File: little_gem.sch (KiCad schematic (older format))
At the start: 11 parts, among them J1 AudioPlug2, U1 LM386

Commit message: Finished sch and pcb
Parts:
- C1, C2, C3: footprint (none) -> Capacitor_THT:C_Rect_L7.2mm_W2.5mm_P5.00mm_FKS2_FKP2_MKS2_MKP2
- C4: value 47 -> 47n; footprint (none) -> Capacitor_THT:C_Rect_L7.2mm_W2.5mm_P5.00mm_FKS2_FKP2_MKS2_MKP2
- C5: value 220n -> 220u; footprint (none) -> Capacitor_THT:CP_Radial_D6.3mm_P2.50mm
- J1: footprint (none) -> Connector_PinHeader_1.00mm:PinHeader_1x02_P1.00mm_Vertical_audio_jack
- LS1: renamed from LS?; footprint (none) -> Connector_PinHeader_1.00mm:PinHeader_1x02_P1.00mm_Vertical
- R1: footprint (none) -> Resistor_THT:R_Axial_DIN0207_L6.3mm_D2.5mm_P10.16mm_Horizontal
- R_GAIN1: renamed from RV1; footprint (none) -> Connector_PinHeader_1.00mm:PinHeader_1x03_P1.00mm_Vertical
- R_VOLUME1: renamed from RV2; footprint (none) -> Connector_PinHeader_1.00mm:PinHeader_1x03_P1.00mm_Vertical
- U1: footprint (none) -> Package_DIP:DIP-8_W7.62mm_Socket_LongPads
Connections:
- net labels added: GND
- net labels removed: GNDA

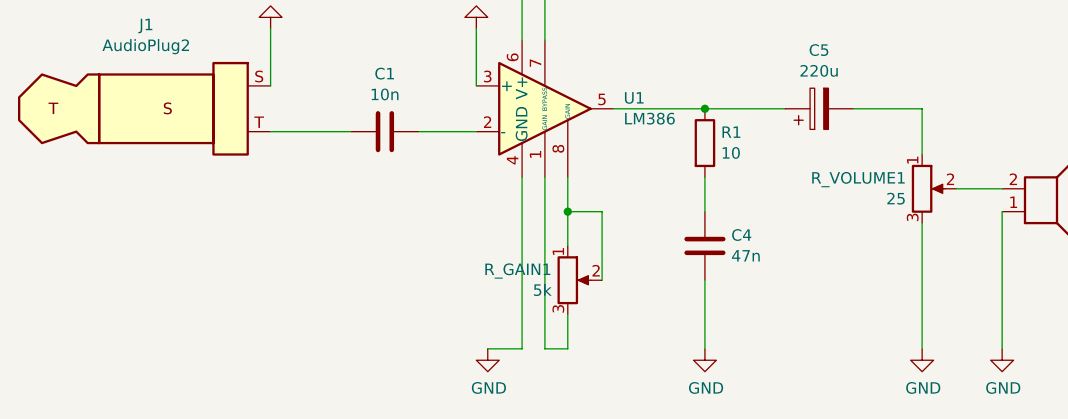
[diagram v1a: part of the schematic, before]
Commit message: replaced footprints for pots and connectors
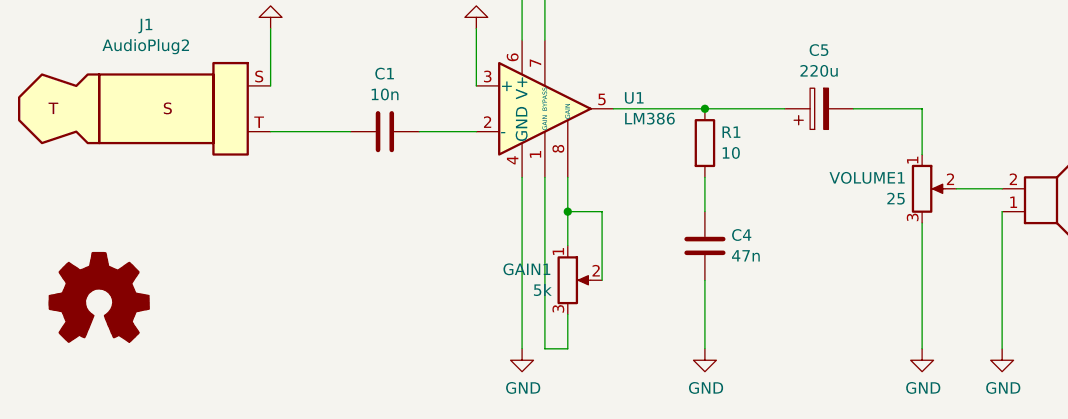
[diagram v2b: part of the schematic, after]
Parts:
- GAIN1: renamed from R_GAIN1; footprint Connector_PinHeader_1.00mm:PinHeader_1x03_P1.00mm_Vertical -> Connector_PinHeader_2.00mm:PinHeader_1x03_P2.00mm_Vertical
- J1: footprint Connector_PinHeader_1.00mm:PinHeader_1x02_P1.00mm_Vertical_audio_jack -> Connector_PinHeader_2.00mm:PinHeader_1x02_P2.00mm_Vertical_LittleGem
- LS1: footprint Connector_PinHeader_1.00mm:PinHeader_1x02_P1.00mm_Vertical -> Connector_PinHeader_2.00mm:PinHeader_1x02_P2.00mm_Vertical
- VOLUME1: renamed from R_VOLUME1; footprint Connector_PinHeader_1.00mm:PinHeader_1x03_P1.00mm_Vertical -> Connector_PinHeader_2.00mm:PinHeader_1x03_P2.00mm_Vertical
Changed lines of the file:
@@
 $EndComp
 $Comp
-L Device:R_POT R_VOLUME1
+L Device:R_POT VOLUME1
 U 1 1 5EF07295
 P 6650 4250
-F 0 "R_VOLUME1" H 6580 4296 50  0000 R CNN
+F 0 "VOLUME1" H 6580 4296 50  0000 R CNN
 F 1 "25" H 6580 4205 50  0000 R CNN
-F 2 "Connector_PinHeader_1.00mm:PinHeader_1x03_P1.00mm_Vertical" H 6650 4250 50  0001 C CNN
+F 2 "Connector_PinHeader_2.00mm:PinHeader_1x03_P2.00mm_Vertical" H 6650 4250 50  0001 C CNN
 F 3 "~" H 6650 4250 50  0001 C CNN
 	1    6650 4250
@@
 	4900 4200 4900 4950
 Wire Wire Line
-	4900 4950 4750 4950
-Wire Wire Line
 	5700 4950 5700 4650
 Wire Wire Line
@@
 	5000 2450 5000 2750
 $Comp
-L power:+9V #PWR0109
+L power:+9V #PWR03
 U 1 1 5EF30250
 P 3950 2750
-F 0 "#PWR0109" H 3950 2600 50  0001 C CNN
+F 0 "#PWR03" H 3950 2600 50  0001 C CNN
 F 1 "+9V" V 3965 2878 50  0000 L CNN
 F 2 "" H 3950 2750 50  0001 C CNN
@@
 	4450 2750 4900 2750
 $Comp
-L power:GND #PWR0102
+L power:GND #PWR07
 U 1 1 5EF434C2
-P 4750 4950
-F 0 "#PWR0102" H 4750 4700 50  0001 C CNN
-F 1 "GND" H 4755 4777 50  0000 C CNN
-F 2 "" H 4750 4950 50  0001 C CNN
-F 3 "" H 4750 4950 50  0001 C CNN
-	1    4750 4950
-	1    0    0    -1
-$EndComp
-$Comp
-L power:GND #PWR0103
+P 4900 4950
+F 0 "#PWR07" H 4900 4700 50  0001 C CNN
+F 1 "GND" H 4905 4777 50  0000 C CNN
+F 2 "" H 4900 4950 50  0001 C CNN
+F 3 "" H 4900 4950 50  0001 C CNN
+	1    4900 4950
+	1    0    0    -1
+$EndComp
+$Comp
+L power:GND #PWR09
 U 1 1 5EF44012
 P 5700 4950
-F 0 "#PWR0103" H 5700 4700 50  0001 C CNN
+F 0 "#PWR09" H 5700 4700 50  0001 C CNN
 F 1 "GND" H 5705 4777 50  0000 C CNN
 F 2 "" H 5700 4950 50  0001 C CNN
@@
 $EndComp
 $Comp
-L power:GND #PWR0104
+L power:GND #PWR010
 U 1 1 5EF44713
 P 6650 4950
-F 0 "#PWR0104" H 6650 4700 50  0001 C CNN
+F 0 "#PWR010" H 6650 4700 50  0001 C CNN
 F 1 "GND" H 6655 4777 50  0000 C CNN
 F 2 "" H 6650 4950 50  0001 C CNN
@@
 $EndComp
 $Comp
-L power:GND #PWR0105
+L power:GND #PWR011
 U 1 1 5EF44C47
 P 7000 4950
-F 0 "#PWR0105" H 7000 4700 50  0001 C CNN
+F 0 "#PWR011" H 7000 4700 50  0001 C CNN
 F 1 "GND" H 7005 4777 50  0000 C CNN
 F 2 "" H 7000 4950 50  0001 C CNN
@@
 $EndComp
 $Comp
-L power:GND #PWR0108
+L power:GND #PWR08
 U 1 1 5EF45800
 P 5000 2450
-F 0 "#PWR0108" H 5000 2200 50  0001 C CNN
+F 0 "#PWR08" H 5000 2200 50  0001 C CNN
 F 1 "GND" H 5005 2277 50  0000 C CNN
 F 2 "" H 5000 2450 50  0001 C CNN
@@
 $EndComp
 $Comp
-L power:GND #PWR0107
+L power:GND #PWR06
 U 1 1 5EF4907C
 P 4700 3550
-F 0 "#PWR0107" H 4700 3300 50  0001 C CNN
+F 0 "#PWR06" H 4700 3300 50  0001 C CNN
 F 1 "GND" H 4705 3377 50  0000 C CNN
 F 2 "" H 4700 3550 50  0001 C CNN
@@
 $EndComp
 $Comp
-L power:GND #PWR0101
+L power:GND #PWR05
 U 1 1 5EF4B5A8
 P 4450 3200
-F 0 "#PWR0101" H 4450 2950 50  0001 C CNN
+F 0 "#PWR05" H 4450 2950 50  0001 C CNN
 F 1 "GND" H 4455 3027 50  0000 C CNN
 F 2 "" H 4450 3200 50  0001 C CNN
@@
 $EndComp
 $Comp
-L power:GND #PWR0106
+L power:GND #PWR01
 U 1 1 5EF4EC5F
 P 3800 3550
-F 0 "#PWR0106" H 3800 3300 50  0001 C CNN
+F 0 "#PWR01" H 3800 3300 50  0001 C CNN
 F 1 "GND" H 3805 3377 50  0000 C CNN
 F 2 "" H 3800 3550 50  0001 C CNN
@@
 $EndComp
 $Comp
-L power:PWR_FLAG #FLG0101
+L power:PWR_FLAG #FLG01
 U 1 1 5EF5745A
 P 3950 1400
-F 0 "#FLG0101" H 3950 1475 50  0001 C CNN
+F 0 "#FLG01" H 3950 1475 50  0001 C CNN
 F 1 "PWR_FLAG" H 3950 1573 50  0000 C CNN
 F 2 "" H 3950 1400 50  0001 C CNN
@@
 $EndComp
 $Comp
-L power:PWR_FLAG #FLG0102
+L power:PWR_FLAG #FLG02
 U 1 1 5EF57882
 P 4300 1400
-F 0 "#FLG0102" H 4300 1475 50  0001 C CNN
+F 0 "#FLG02" H 4300 1475 50  0001 C CNN
 F 1 "PWR_FLAG" H 4300 1573 50  0000 C CNN
 F 2 "" H 4300 1400 50  0001 C CNN
@@
 $EndComp
 $Comp
-L power:+9V #PWR0110
+L power:+9V #PWR02
 U 1 1 5EF57D46
 P 3950 1400
-F 0 "#PWR0110" H 3950 1250 50  0001 C CNN
+F 0 "#PWR02" H 3950 1250 50  0001 C CNN
 F 1 "+9V" V 3965 1528 50  0000 L CNN
 F 2 "" H 3950 1400 50  0001 C CNN
@@
 $EndComp
 $Comp
-L power:GND #PWR0111
+L power:GND #PWR04
 U 1 1 5EF585B3
 P 4300 1400
-F 0 "#PWR0111" H 4300 1150 50  0001 C CNN
+F 0 "#PWR04" H 4300 1150 50  0001 C CNN
 F 1 "GND" H 4305 1227 50  0000 C CNN
 F 2 "" H 4300 1400 50  0001 C CNN
@@
 F 0 "J1" H 3257 4267 50  0000 C CNN
 F 1 "AudioPlug2" H 3257 4176 50  0000 C CNN
-F 2 "Connector_PinHeader_1.00mm:PinHeader_1x02_P1.00mm_Vertical_audio_jack" H 3550 3850 50  0001 C CNN
+F 2 "Connector_PinHeader_2.00mm:PinHeader_1x02_P2.00mm_Vertical_LittleGem" H 3550 3850 50  0001 C CNN
 F 3 "~" H 3550 3850 50  0001 C CNN
 	1    3200 3900
@@
 F 0 "LS1" H 7370 4346 50  0000 L CNN
 F 1 "Speaker" H 7370 4255 50  0000 L CNN
-F 2 "Connector_PinHeader_1.00mm:PinHeader_1x02_P1.00mm_Vertical" H 7200 4150 50  0001 C CNN
+F 2 "Connector_PinHeader_2.00mm:PinHeader_1x02_P2.00mm_Vertical" H 7200 4150 50  0001 C CNN
 F 3 "~" H 7190 4300 50  0001 C CNN
 	1    7200 4350
@@
 $EndComp
 $Comp
-L Device:R_POT R_GAIN1
+L Graphic:Logo_Open_Hardware_Small #LOGO1
+U 1 1 5F1CB9EF
+P 3050 4750
+F 0 "#LOGO1" H 3050 5025 50  0001 C CNN
+F 1 "Logo_Open_Hardware_Small" H 3050 4525 50  0001 C CNN
+F 2 "" H 3050 4750 50  0001 C CNN
+F 3 "~" H 3050 4750 50  0001 C CNN
+	1    3050 4750
+	1    0    0    -1
+$EndComp
+$Comp
+L Device:R_POT GAIN1
 U 1 1 5EF0806F
 P 5100 4650
-F 0 "R_GAIN1" H 5030 4696 50  0000 R CNN
+F 0 "GAIN1" H 5030 4696 50  0000 R CNN
 F 1 "5k" H 5030 4605 50  0000 R CNN
-F 2 "Connector_PinHeader_1.00mm:PinHeader_1x03_P1.00mm_Vertical" H 5100 4650 50  0001 C CNN
+F 2 "Connector_PinHeader_2.00mm:PinHeader_1x03_P2.00mm_Vertical" H 5100 4650 50  0001 C CNN
 F 3 "~" H 5100 4650 50  0001 C CNN
 	1    5100 4650

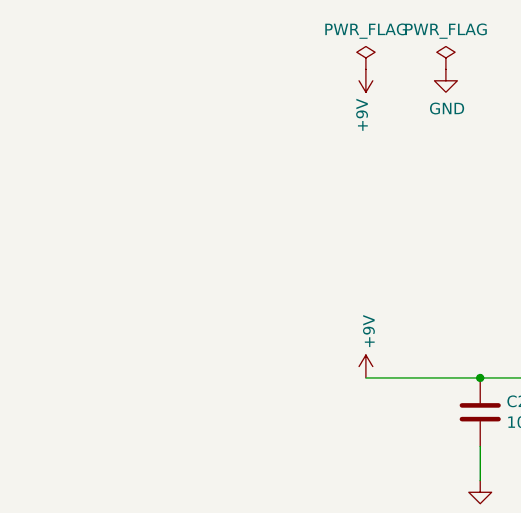
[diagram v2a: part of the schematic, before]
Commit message: added power pins
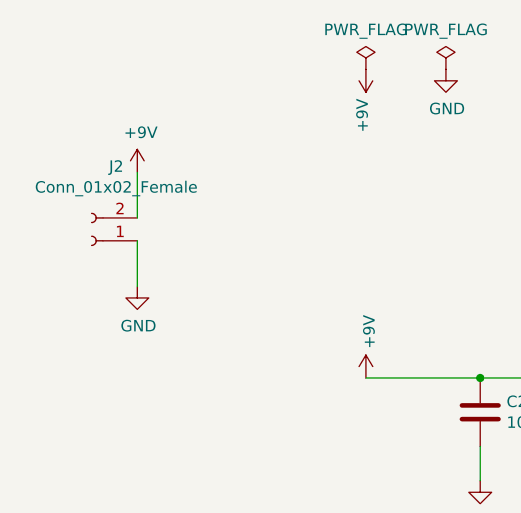
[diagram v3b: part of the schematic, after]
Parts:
- added J2: Conn_01x02_Female, Connector_PinHeader_2.54mm:PinHeader_2x01_P2.54mm_Vertical, symbol Connector:Conn_01x02_Female
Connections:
- net +9V: now also J2.2 (Pin_2)
- net GND: now also J2.1 (Pin_1)
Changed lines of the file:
@@
 	1    0    0    -1
 $EndComp
+$Comp
+L Connector:Conn_01x02_Female J2
+U 1 1 5F4A2F4F
+P 2750 2150
+F 0 "J2" H 2642 1825 50  0000 C CNN
+F 1 "Conn_01x02_Female" H 2642 1916 50  0000 C CNN
+F 2 "Connector_PinHeader_2.54mm:PinHeader_2x01_P2.54mm_Vertical" H 2750 2150 50  0001 C CNN
+F 3 "~" H 2750 2150 50  0001 C CNN
+	1    2750 2150
+	-1   0    0    1
+$EndComp
+$Comp
+L power:+9V #PWR012
+U 1 1 5F4A8CE8
+P 2950 1850
+F 0 "#PWR012" H 2950 1700 50  0001 C CNN
+F 1 "+9V" H 2965 2023 50  0000 C CNN
+F 2 "" H 2950 1850 50  0001 C CNN
+F 3 "" H 2950 1850 50  0001 C CNN
+	1    2950 1850
+	1    0    0    -1
+$EndComp
+$Comp
+L power:GND #PWR013
+U 1 1 5F4A9618
+P 2950 2350
+F 0 "#PWR013" H 2950 2100 50  0001 C CNN
+F 1 "GND" H 2955 2177 50  0000 C CNN
+F 2 "" H 2950 2350 50  0001 C CNN
+F 3 "" H 2950 2350 50  0001 C CNN
+	1    2950 2350
+	1    0    0    -1
+$EndComp
+Wire Wire Line
+	2950 2050 2950 1850
+Wire Wire Line
+	2950 2150 2950 2350
 $EndSCHEMATC

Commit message: changed pot footprints
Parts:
- GAIN1, VOLUME1: footprint Connector_PinHeader_2.00mm:PinHeader_1x03_P2.00mm_Vertical -> Connector_PinHeader_2.54mm:PinHeader_1x03_P2.54mm_Vertical
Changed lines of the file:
@@
 F 0 "VOLUME1" H 6580 4296 50  0000 R CNN
 F 1 "25" H 6580 4205 50  0000 R CNN
-F 2 "Connector_PinHeader_2.00mm:PinHeader_1x03_P2.00mm_Vertical" H 6650 4250 50  0001 C CNN
+F 2 "Connector_PinHeader_2.54mm:PinHeader_1x03_P2.54mm_Vertical" H 6650 4250 50  0001 C CNN
 F 3 "~" H 6650 4250 50  0001 C CNN
 	1    6650 4250
@@
 F 0 "GAIN1" H 5030 4696 50  0000 R CNN
 F 1 "5k" H 5030 4605 50  0000 R CNN
-F 2 "Connector_PinHeader_2.00mm:PinHeader_1x03_P2.00mm_Vertical" H 5100 4650 50  0001 C CNN
+F 2 "Connector_PinHeader_2.54mm:PinHeader_1x03_P2.54mm_Vertical" H 5100 4650 50  0001 C CNN
 F 3 "~" H 5100 4650 50  0001 C CNN
 	1    5100 4650

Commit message: Fixed footprints
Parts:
- removed J1: AudioPlug2, Connector_PinHeader_2.00mm:PinHeader_1x02_P2.00mm_Vertical_LittleGem, symbol Connector:AudioPlug2
- added J1: Conn_01x02_Female, Connector_PinHeader_2.54mm:PinHeader_1x02_P2.54mm_Vertical, symbol Connector:Conn_01x02_Female
- LS1: footprint Connector_PinHeader_2.00mm:PinHeader_1x02_P2.00mm_Vertical -> Connector_PinHeader_2.54mm:PinHeader_1x02_P2.54mm_Vertical
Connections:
- net GND: now also J1.1 (Pin_1)
- net at C1.2: now also J1.2 (Pin_2)
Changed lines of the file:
@@
 	4700 3550 4700 3800
 Wire Wire Line
-	3800 3550 3800 3800
+	3800 3650 3800 3900
 Wire Wire Line
 	4450 3200 4450 3050
@@
 L power:GND #PWR01
 U 1 1 5EF4EC5F
-P 3800 3550
-F 0 "#PWR01" H 3800 3300 50  0001 C CNN
-F 1 "GND" H 3805 3377 50  0000 C CNN
-F 2 "" H 3800 3550 50  0001 C CNN
-F 3 "" H 3800 3550 50  0001 C CNN
-	1    3800 3550
+P 3800 3650
+F 0 "#PWR01" H 3800 3400 50  0001 C CNN
+F 1 "GND" H 3805 3477 50  0000 C CNN
+F 2 "" H 3800 3650 50  0001 C CNN
+F 3 "" H 3800 3650 50  0001 C CNN
+	1    3800 3650
 	-1   0    0    1
 $EndComp
@@
 $EndComp
 $Comp
-L Connector:AudioPlug2 J1
-U 1 1 5EF095AF
-P 3200 3900
-F 0 "J1" H 3257 4267 50  0000 C CNN
-F 1 "AudioPlug2" H 3257 4176 50  0000 C CNN
-F 2 "Connector_PinHeader_2.00mm:PinHeader_1x02_P2.00mm_Vertical_LittleGem" H 3550 3850 50  0001 C CNN
-F 3 "~" H 3550 3850 50  0001 C CNN
-	1    3200 3900
-	1    0    0    -1
-$EndComp
-$Comp
 L Device:Speaker LS1
 U 1 1 5EF184C9
@@
 F 0 "LS1" H 7370 4346 50  0000 L CNN
 F 1 "Speaker" H 7370 4255 50  0000 L CNN
-F 2 "Connector_PinHeader_2.00mm:PinHeader_1x02_P2.00mm_Vertical" H 7200 4150 50  0001 C CNN
+F 2 "Connector_PinHeader_2.54mm:PinHeader_1x02_P2.54mm_Vertical" H 7200 4150 50  0001 C CNN
 F 3 "~" H 7190 4300 50  0001 C CNN
 	1    7200 4350
@@
 Wire Wire Line
 	2950 2150 2950 2350
+$Comp
+L Connector:Conn_01x02_Female J1
+U 1 1 5F4FF7F7
+P 3600 3900
+F 0 "J1" H 3492 3575 50  0000 C CNN
+F 1 "Conn_01x02_Female" H 3492 3666 50  0000 C CNN
+F 2 "Connector_PinHeader_2.54mm:PinHeader_1x02_P2.54mm_Vertical" H 3600 3900 50  0001 C CNN
+F 3 "~" H 3600 3900 50  0001 C CNN
+	1    3600 3900
+	-1   0    0    -1
+$EndComp
 $EndSCHEMATC

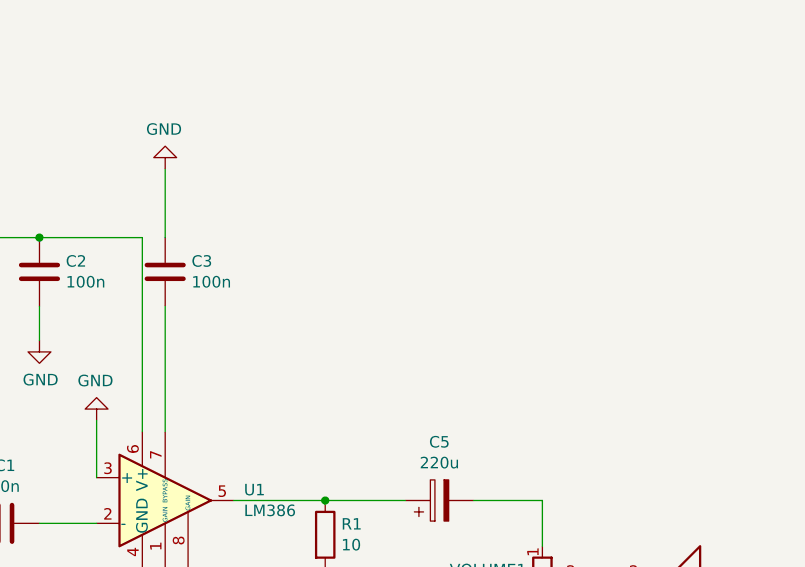
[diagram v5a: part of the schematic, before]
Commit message: added led
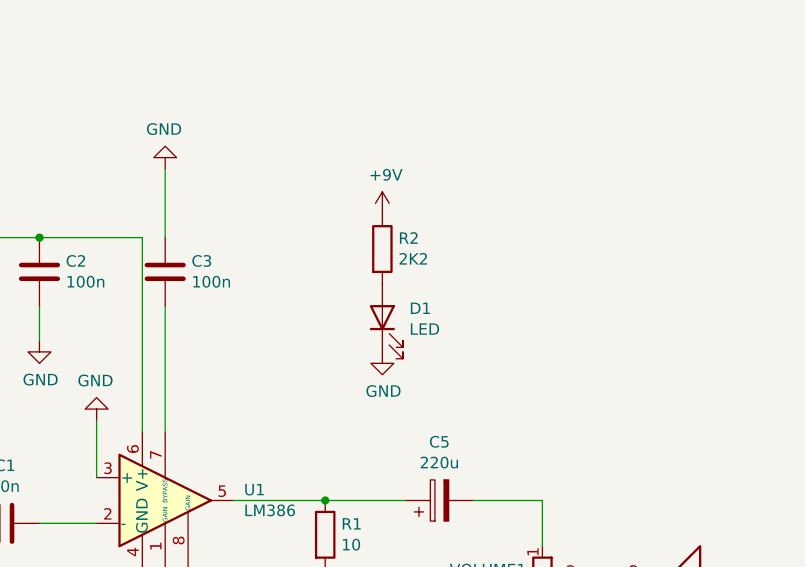
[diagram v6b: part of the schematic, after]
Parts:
- added D1: LED, LED_THT:LED_D3.0mm, symbol Device:LED
- added R2: 2K2, Resistor_THT:R_Axial_DIN0207_L6.3mm_D2.5mm_P10.16mm_Horizontal, symbol Device:R
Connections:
- net +9V: now also R2.1
- net GND: now also D1.1 (K)
- new net: D1.2 (A), R2.2
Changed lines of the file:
@@
 	-1   0    0    -1
 $EndComp
+$Comp
+L Device:LED D1
+U 1 1 5F5227E7
+P 5950 3100
+F 0 "D1" V 5989 2982 50  0000 R CNN
+F 1 "LED" V 5898 2982 50  0000 R CNN
+F 2 "LED_THT:LED_D3.0mm" H 5950 3100 50  0001 C CNN
+F 3 "~" H 5950 3100 50  0001 C CNN
+	1    5950 3100
+	0    -1   -1   0
+$EndComp
+$Comp
+L Device:R R2
+U 1 1 5F524415
+P 5950 2800
+F 0 "R2" H 6020 2846 50  0000 L CNN
+F 1 "2K2" H 6020 2755 50  0000 L CNN
+F 2 "Resistor_THT:R_Axial_DIN0207_L6.3mm_D2.5mm_P10.16mm_Horizontal" V 5880 2800 50  0001 C CNN
+F 3 "~" H 5950 2800 50  0001 C CNN
+	1    5950 2800
+	1    0    0    -1
+$EndComp
+$Comp
+L power:+9V #PWR014
+U 1 1 5F524D56
+P 5950 2650
+F 0 "#PWR014" H 5950 2500 50  0001 C CNN
+F 1 "+9V" H 5965 2823 50  0000 C CNN
+F 2 "" H 5950 2650 50  0001 C CNN
+F 3 "" H 5950 2650 50  0001 C CNN
+	1    5950 2650
+	1    0    0    -1
+$EndComp
+$Comp
+L power:GND #PWR015
+U 1 1 5F5251B2
+P 5950 3250
+F 0 "#PWR015" H 5950 3000 50  0001 C CNN
+F 1 "GND" H 5955 3077 50  0000 C CNN
+F 2 "" H 5950 3250 50  0001 C CNN
+F 3 "" H 5950 3250 50  0001 C CNN
+	1    5950 3250
+	1    0    0    -1
+$EndComp
 $EndSCHEMATC

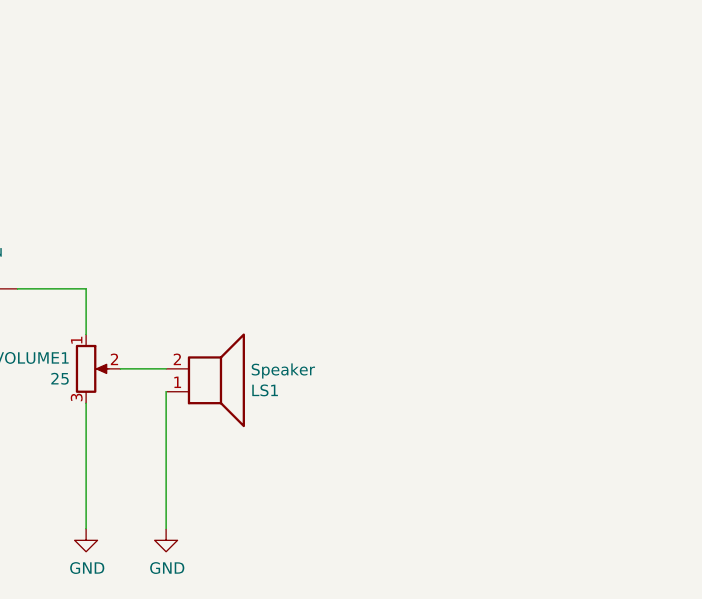
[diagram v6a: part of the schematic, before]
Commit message: added 3.5mm jack
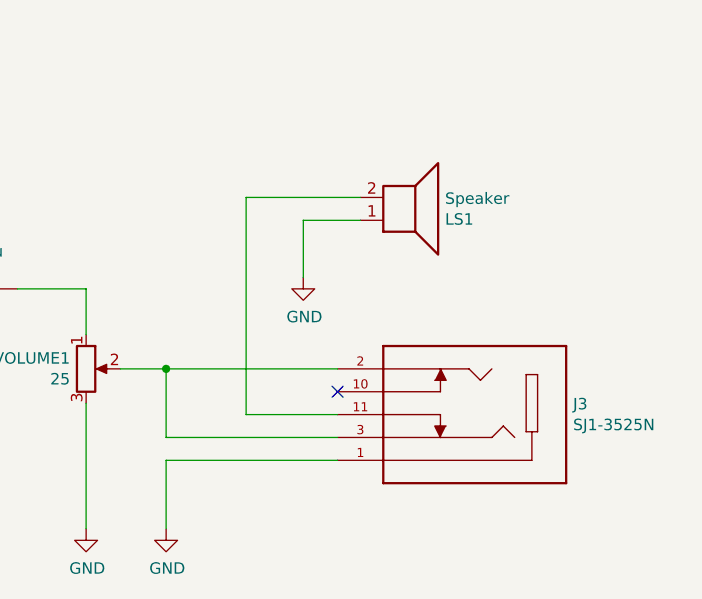
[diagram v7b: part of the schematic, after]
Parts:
- added J3: SJ1-3525N, CUI_SJ1-3525N, symbol 3_5mm:SJ1-3525N
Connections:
- net GND: now also J3.1
- net at VOLUME1.2: now also J3.2, J3.3; no longer LS1.2
- new net: J3.11, LS1.2
- no-connect marks 0 -> 1
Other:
- moved on the sheet: LS1
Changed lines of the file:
@@
 	6650 3900 6650 4100
-Wire Wire Line
-	6800 4250 7000 4250
 Wire Wire Line
 	5700 4200 5700 4350
@@
 	6650 4950 6650 4400
 Wire Wire Line
-	7000 4350 7000 4950
+	7000 4650 7000 4950
 Wire Wire Line
 	5000 2450 5000 2750
@@
 L Device:Speaker LS1
 U 1 1 5EF184C9
-P 7200 4350
-F 0 "LS1" H 7370 4346 50  0000 L CNN
-F 1 "Speaker" H 7370 4255 50  0000 L CNN
-F 2 "Connector_PinHeader_2.54mm:PinHeader_1x02_P2.54mm_Vertical" H 7200 4150 50  0001 C CNN
-F 3 "~" H 7190 4300 50  0001 C CNN
-	1    7200 4350
+P 8050 3600
+F 0 "LS1" H 8220 3596 50  0000 L CNN
+F 1 "Speaker" H 8220 3505 50  0000 L CNN
+F 2 "Connector_PinHeader_2.54mm:PinHeader_1x02_P2.54mm_Vertical" H 8050 3400 50  0001 C CNN
+F 3 "~" H 8040 3550 50  0001 C CNN
+	1    8050 3600
 	1    0    0    1
 $EndComp
@@
 	1    0    0    -1
 $EndComp
+$Comp
+L 3_5mm:SJ1-3525N J3
+U 1 1 5F513EAD
+P 8350 4450
+F 0 "J3" H 7920 4404 50  0000 R CNN
+F 1 "SJ1-3525N" H 7920 4495 50  0000 R CNN
+F 2 "CUI_SJ1-3525N" H 8350 4450 50  0001 L BNN
+F 3 "Manufacturer recommendation" H 8350 4450 50  0001 L BNN
+F 4 "CUI" H 8350 4450 50  0001 L BNN "Field4"
+F 5 "1.02" H 8350 4450 50  0001 L BNN "Field5"
+	1    8350 4450
+	-1   0    0    1
+$EndComp
+Wire Wire Line
+	7000 4650 7750 4650
+Wire Wire Line
+	6800 4250 7000 4250
+Wire Wire Line
+	7750 4550 7000 4550
+Wire Wire Line
+	7000 4550 7000 4250
+Connection ~ 7000 4250
+Wire Wire Line
+	7000 4250 7750 4250
+Wire Wire Line
+	7850 3500 7350 3500
+Wire Wire Line
+	7350 3500 7350 4450
+Wire Wire Line
+	7350 4450 7750 4450
+$Comp
+L power:GND #PWR0101
+U 1 1 5F537EBA
+P 7600 3850
+F 0 "#PWR0101" H 7600 3600 50  0001 C CNN
+F 1 "GND" H 7605 3677 50  0000 C CNN
+F 2 "" H 7600 3850 50  0001 C CNN
+F 3 "" H 7600 3850 50  0001 C CNN
+	1    7600 3850
+	1    0    0    -1
+$EndComp
+Wire Wire Line
+	7600 3850 7600 3600
+Wire Wire Line
+	7600 3600 7850 3600
+NoConn ~ 7750 4350
 $EndSCHEMATC
